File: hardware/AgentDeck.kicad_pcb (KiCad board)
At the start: 4 copper layers, 95 x 95 mm, 101 parts, among them J1 USB-C, J2 SWD, SW1 K1, SW10 K10, SW11 K11, SW12 K12, SW13 BOOTSEL, SW14 CONN-SMD_HOTPLUGPAKAGE__C9900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, SW2 K2, SW3 K3, SW4 K4, SW5 K5, SW6 K6, SW7 K7, SW8 K8, SW9 K9, U1 RP2040, U2 W25Q128JVSIQ, U3 AMS1117-3.3, U4 74AHCT1G125, U6 USBLC6-2SC6, Y1 ABM8-272-T3

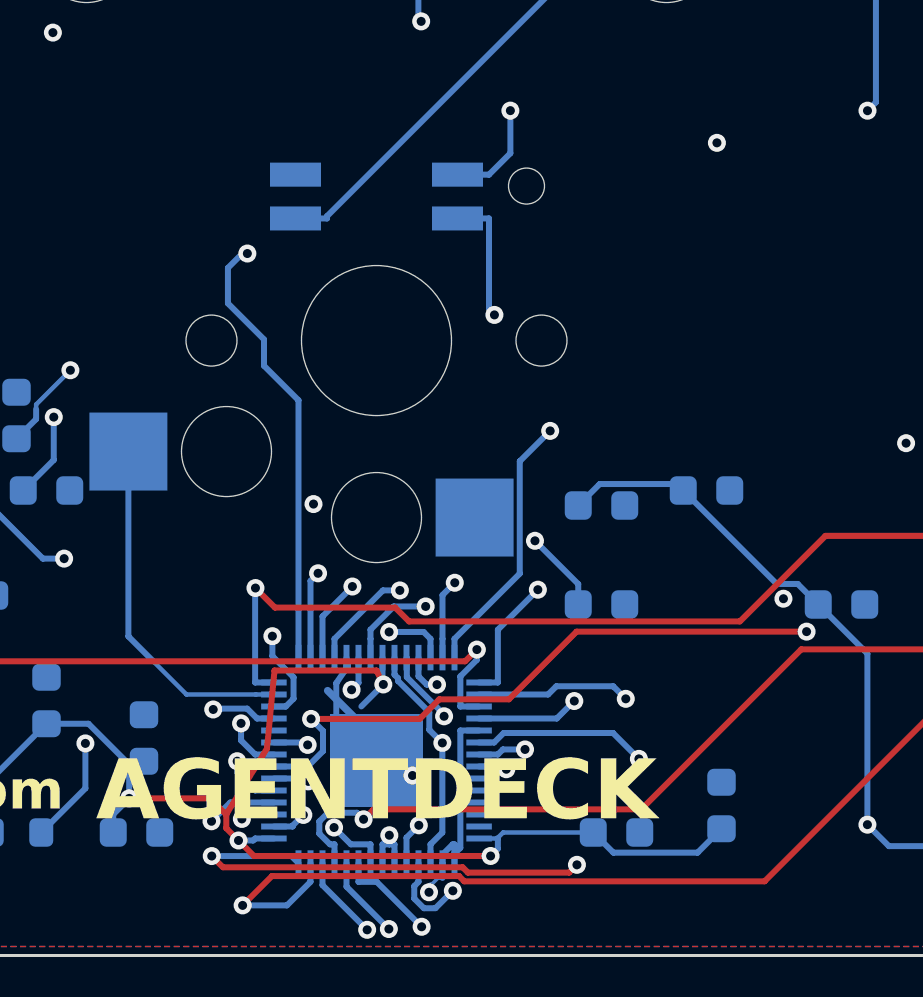
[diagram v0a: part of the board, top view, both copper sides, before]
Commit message: restore copper zones
Deleted then re-added the 5 pours (user request). User's GUI routing between
delete and restore closed the pin-19 GND and pad-10 +3V3 connections that
scripts could not. With pours refilled: 0 DRC errors, 1 unconnected (K7 -
an In1 switch escape needs 1 via up to the B.Cu net, blocked by the +3V3
wall + K4/K9/AUX3 congestion; a push-shove GUI job).
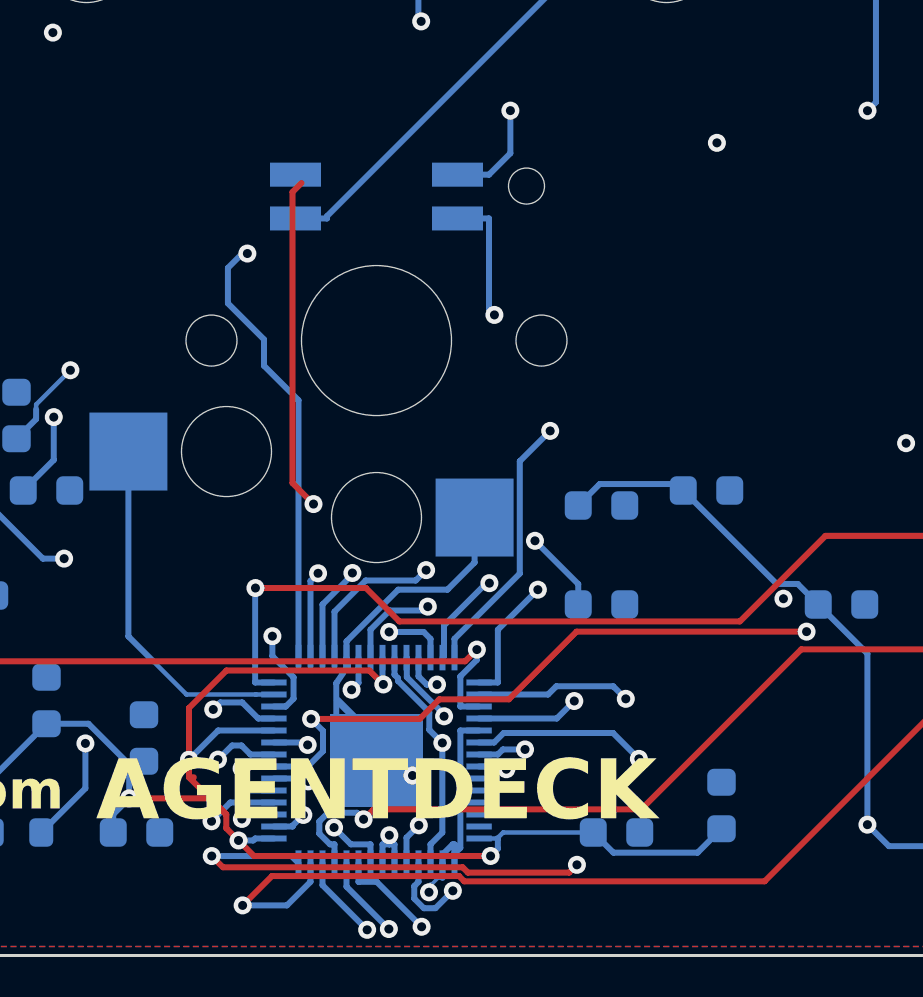
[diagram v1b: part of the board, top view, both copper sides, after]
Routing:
- net GND: track 10.5 -> 28.5 mm
- net +3V3: track 182.3 -> 186.8 mm, vias 11 -> 12
- net ENC_SW: track 98.7 -> 99.6 mm
- net JOY_A: track 97.8 -> 98.4 mm

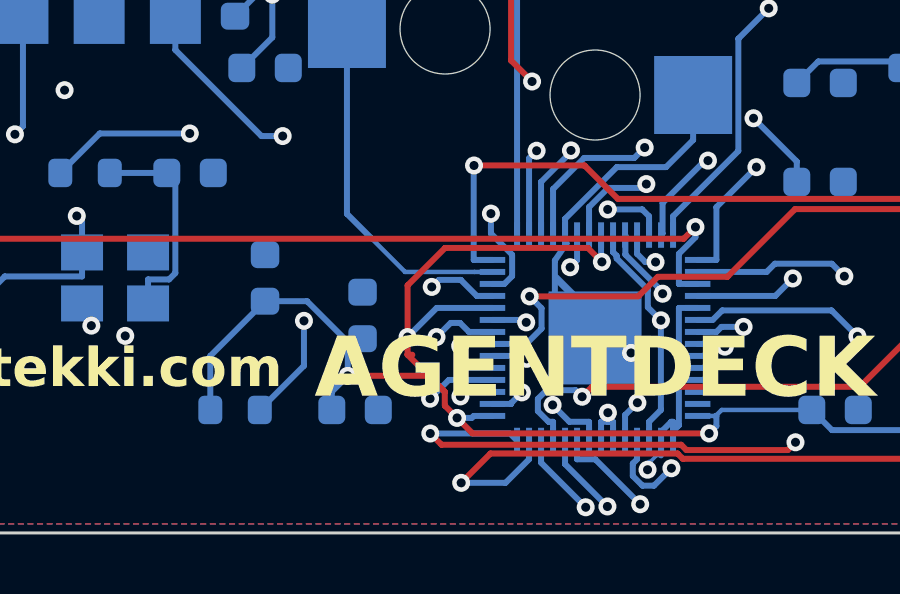
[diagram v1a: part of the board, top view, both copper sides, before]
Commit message: complete v1 routing
Board fully routed: 0 DRC errors, 0 unconnected, 92 nets complete on 95x95mm.
Final K7 escape routed in pcbnew (push-shove); zones refilled to clear the
stale-fill overlaps. Gerbers + drill regenerated for the finished board.

Remaining 42 warnings are non-blocking: JLC footprint-lib notes (17),
pour islands / isolated copper (15, cosmetic), courtyard overlaps (3),
annular/padstack/thermal (pre-existing class). Manufacturable state.
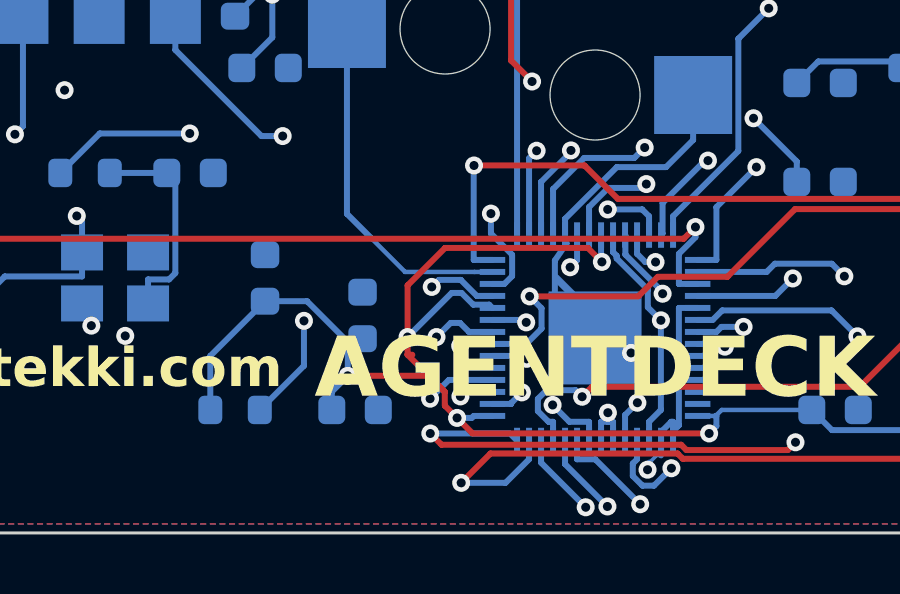
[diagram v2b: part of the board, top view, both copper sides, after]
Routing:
- net K7: track 59.0 -> 59.7 mm
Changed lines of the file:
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@@
-	)
-	(segment
-		(start 41.58 85)
-		(end 39.7207 85)
-		(width 0.2)
-		(layer "B.Cu")
-		(net "+3V3")
 	)
 	(segment
@@
 	)
 	(segment
+		(start 41.47 84.89)
+		(end 40.939128 84.89)
+		(width 0.2)
+		(layer "B.Cu")
+		(net "+3V3")
+	)
+	(segment
 		(start 65.3961 89.0283)
 		(end 65.6006 88.8238)
@@
 	)
 	(segment
-		(start 39.7207 85)
-		(end 38.75 85.9707)
-		(width 0.2)
-		(layer "B.Cu")
-		(net "+3V3")
-	)
-	(segment
 		(start 64.8915 88.855)
 		(end 64.9013 88.8452)
@@
 	)
 	(segment
+		(start 41.58 85)
+		(end 41.47 84.89)
+		(width 0.2)
+		(layer "B.Cu")
+		(net "+3V3")
+	)
+	(segment
 		(start 47.2 89.42)
 		(end 47.2 89.9152)
@@
 	)
 	(segment
+		(start 40.549128 84.5)
+		(end 40.2207 84.5)
+		(width 0.2)
+		(layer "B.Cu")
+		(net "+3V3")
+	)
+	(segment
 		(start 19.7125 85.2104)
 		(end 19.2111 84.7089)
+		(width 0.2)
+		(layer "B.Cu")
+		(net "+3V3")
+	)
+	(segment
+		(start 40.939128 84.89)
+		(end 40.549128 84.5)
 		(width 0.2)
 		(layer "B.Cu")
@@
 	)
 	(segment
+		(start 40.2207 84.5)
+		(end 38.75 85.9707)
+		(width 0.2)
+		(layer "B.Cu")
+		(net "+3V3")
+	)
+	(segment
 		(start 34 84.775)
 		(end 35.3996 84.775)
@@
 	)
 	(segment
+		(start 34.2132 61.7368)
+		(end 37.0487 64.5723)
+		(width 0.2)
+		(layer "In1.Cu")
+		(net "K7")
+	)
+	(segment
 		(start 37.0487 64.5723)
-		(end 34.2132 61.7368)
+		(end 37.0487 83.304063)
 		(width 0.2)
 		(layer "In1.Cu")
@@
 	)
 	(segment
-		(start 40.52374 84.897735)
-		(end 40.52374 84.798306)
-		(width 0.2)
-		(layer "In1.Cu")
-		(net "K7")
-	)
-	(segment
-		(start 37.0487 80.857)
-		(end 37.0487 64.5723)
-		(width 0.2)
-		(layer "In1.Cu")
-		(net "K7")
-	)
-	(segment
-		(start 40.4852 84.759766)
-		(end 40.4852 84.2935)
-		(width 0.2)
-		(layer "In1.Cu")
-		(net "K7")
-	)
-	(segment
-		(start 40.4852 84.2935)
-		(end 37.0487 80.857)
-		(width 0.2)
-		(layer "In1.Cu")
-		(net "K7")
-	)
-	(segment
-		(start 40.52374 84.798306)
-		(end 40.4852 84.759766)
-		(width 0.2)
-		(layer "In1.Cu")
+		(start 37.0487 83.304063)
+		(end 39.715336 85.970699)
+		(width 0.2)
+		(layer "In1.Cu")
